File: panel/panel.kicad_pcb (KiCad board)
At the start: 2 copper layers, 60.4 x 128.4 mm, 48 parts

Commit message: Ver 2.0 of board.
Also major advances in code.
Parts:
- added H46: MountingHole, panel:3mmLED, F.Cu at (111.5, 59.5)
- added H47: MountingHole, panel:3mmLED, F.Cu at (111.5, 71.5)
- added H48: MountingHole, panel:3mmLED, F.Cu at (111.5, 83.5)
- added H49: MountingHole, panel:3mmLED, F.Cu at (111.5, 95.5)
- added H50: MountingHole, panel:3mmLED, F.Cu at (111.5, 109.5)
- added H51: MountingHole, panel:3mmLED, F.Cu at (111.5, 121.5)
- added H52: MountingHole, panel:3mmLED, F.Cu at (111.5, 133.5)
- added H53: MountingHole, panel:3mmLED, F.Cu at (111.5, 145.5)
- added H54: MountingHole, panel:3mmLED, F.Cu at (111.5, 64.5)
- added H55: MountingHole, panel:3mmLED, F.Cu at (111.5, 76.5)
- added H56: MountingHole, panel:3mmLED, F.Cu at (111.5, 88.5)
- added H57: MountingHole, panel:3mmLED, F.Cu at (111.5, 100.5)
- added H58: MountingHole, panel:3mmLED, F.Cu at (111.5, 114.5)
- added H59: MountingHole, panel:3mmLED, F.Cu at (111.5, 126.5)
- added H60: MountingHole, panel:3mmLED, F.Cu at (111.8, 138.5)
- added H61: MountingHole, panel:3mmLED, F.Cu at (111.5, 150.5)
- added H62: MountingHole, panel:3mmLED, F.Cu at (84.1, 125.7)
- added H63: MountingHole, panel:3mmLED, F.Cu at (84.1, 149.7)
- moved H2 10.2 mm to (108.2, 43.8)
- moved H3 10.2 mm to (108.2, 166.2)
- moved GR2 10.0 mm to (108.0, 158.3)
- moved H18 10.0 mm to (117.0, 53.0)
- moved H19 10.0 mm to (117.0, 157.0)
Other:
- board size 60.4 x 128.4 mm -> 70.8 x 128.4 mm
- board text added: "14 HP -- WiFi Enabled"
- board text added: "v2.0"
- board text removed: "12 HP -- WiFi Enabled"
- board text removed: "Clip"
- board text removed: "v1.0"

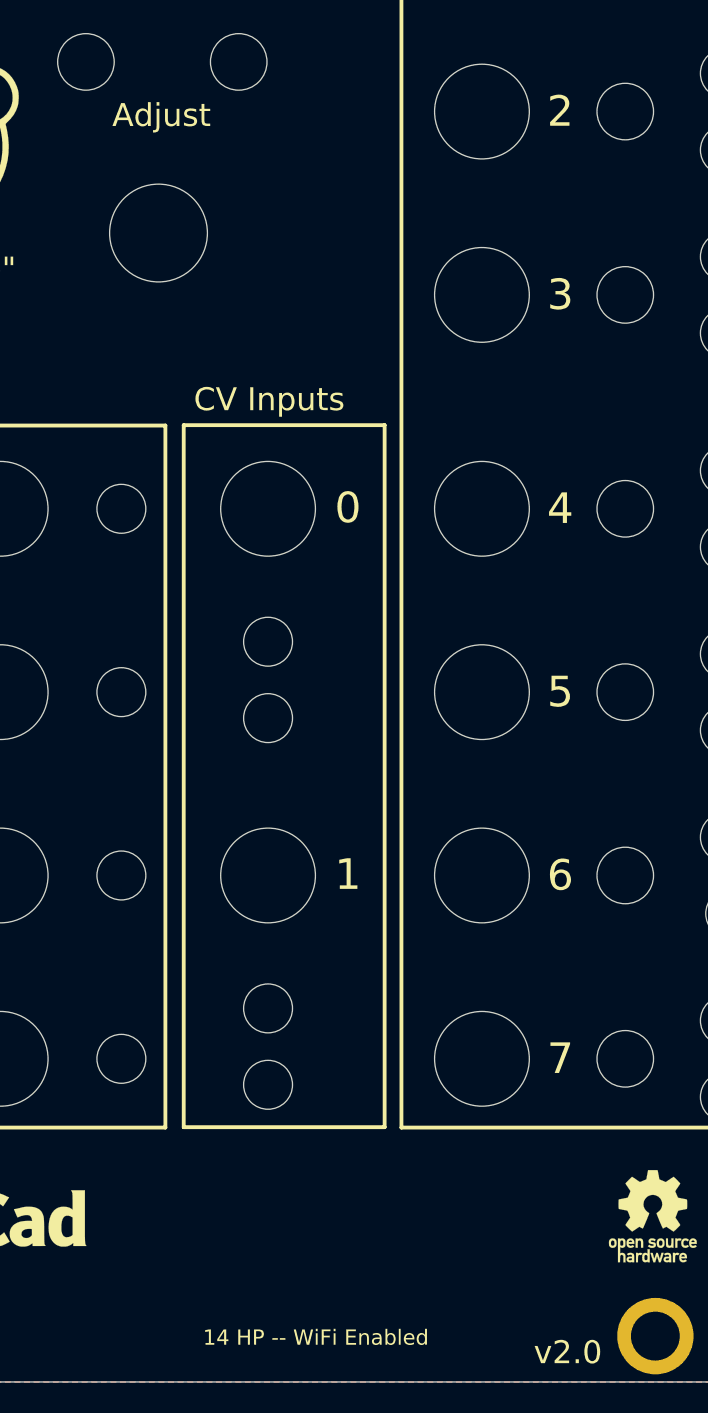
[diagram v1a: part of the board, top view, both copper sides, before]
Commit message: Software v2.2
Removes unneeded files.
Adds pre-flight handler in WiFi do_server();
Removes debug printouts.
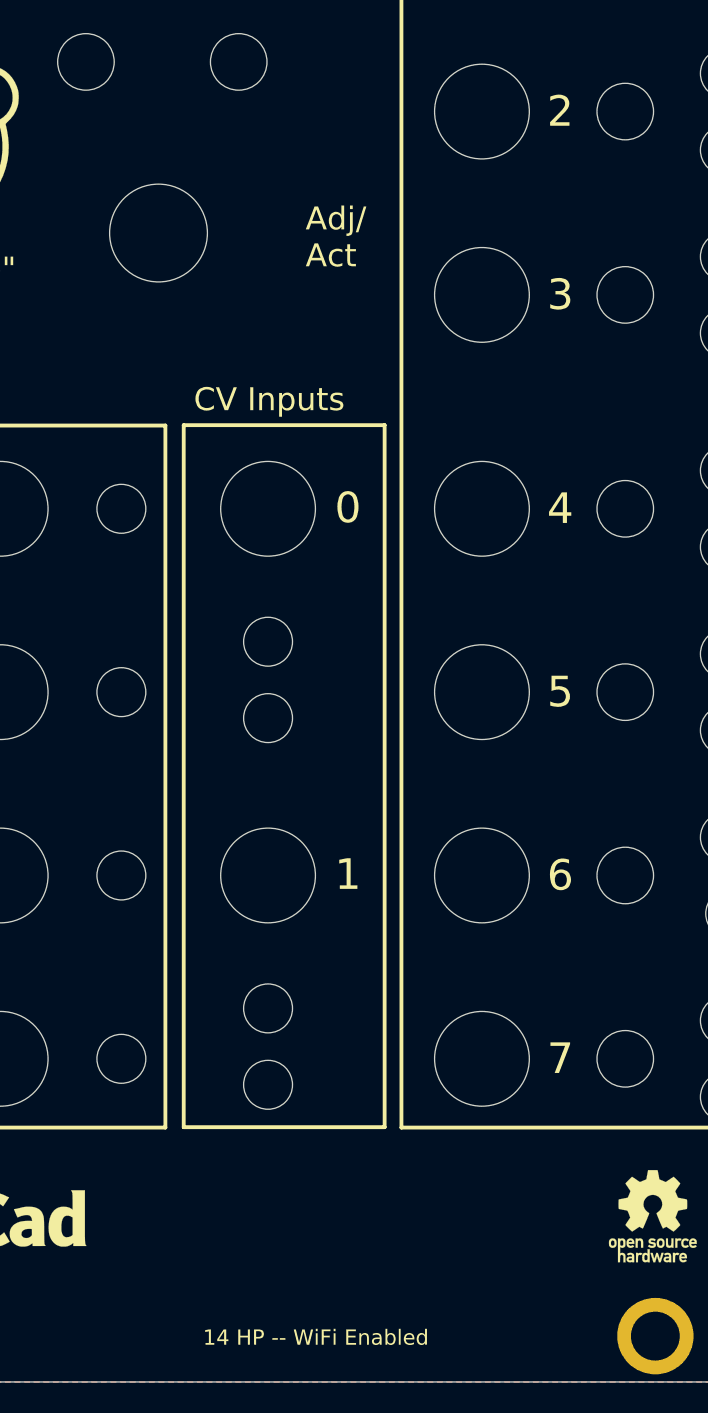
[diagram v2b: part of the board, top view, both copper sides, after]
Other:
- board text added: "Adj/ Act"
- board text added: "Greenface Labs {dblquote}The Bonkulator{dblquote} Panel: v1.1"
- board text removed: "Adjust"
- board text removed: "Greenface Labs {dblquote}The Bonkulator{dblquote} v1.0"
- board text removed: "v2.0"
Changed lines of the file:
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@@
   (gr_line (start 62.7 56.75) (end 62.7 71.75) (layer "Edge.Cuts") (width 0.05))
   (gr_line (start 88.7 71.75) (end 88.7 56.75) (layer "Edge.Cuts") (width 0.05))
-  (gr_text "Greenface Labs\n{dblquote}The Bonkulator{dblquote}\nv1.0" (at 85.75 162.5) (layer "B.SilkS")
+  (gr_text "Greenface Labs\n{dblquote}The Bonkulator{dblquote}\nPanel: v1.1" (at 85.75 162.5) (layer "B.SilkS")
     (effects (font (size 1.5 1.5) (thickness 0.25)) (justify mirror))
   )
@@
     (effects (font (size 2 2) (thickness 0.3)))
   )
-  (gr_text "Adjust" (at 75.9 86.25) (layer "F.SilkS")
-    (effects (font (size 1.5 1.5) (thickness 0.3)))
-  )
-  (gr_text "v2.0" (at 102.5 167.225) (layer "F.SilkS")
-    (effects (font (size 1.5 1.5) (thickness 0.15)))
+  (gr_text "Adj/\nAct" (at 85.325 94.225) (layer "F.SilkS")
+    (effects (font (size 1.5 1.5) (thickness 0.3)) (justify left))
   )
   (gr_text "<" (at 53.05 68 90) (layer "F.SilkS")

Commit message: Updates panel
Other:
- outline, holes or cut-outs redrawn
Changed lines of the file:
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@@
   )
   (paper "A4")
+  (title_block
+    (rev "2.1")
+  )
   (layers
     (0 "F.Cu" signal)
@@
     (pad "" np_thru_hole circle (at 1.27 0) (size 3.2 3.2) (drill 3.2) (layers *.Cu *.Mask))
   )
-  (gr_line (start 62.4 72.05) (end 62.4 56.45) (layer "F.SilkS") (width 0.5))
+  (gr_line (start 62.4 71) (end 62.4 56.45) (layer "F.SilkS") (width 0.5))
   (gr_rect (start 91.6 56.4) (end 119.55 152.5) (layer "F.SilkS") (width 0.25) (fill none))
   (gr_rect (start 51.1 106.55) (end 76.15 152.5) (layer "F.SilkS") (width 0.25) (fill none))
-  (gr_line (start 89 56.45) (end 89 72.05) (layer "F.SilkS") (width 0.5))
+  (gr_line (start 89 56.45) (end 89 71) (layer "F.SilkS") (width 0.5))
   (gr_rect (start 77.35 106.525) (end 90.5 152.475) (layer "F.SilkS") (width 0.25) (fill none))
   (gr_line (start 62.4 56.45) (end 89 56.45) (layer "F.SilkS") (width 0.5))
-  (gr_line (start 89 72.05) (end 62.4 72.05) (layer "F.SilkS") (width 0.5))
+  (gr_line (start 89 71.05) (end 62.4 71.05) (layer "F.SilkS") (width 0.5))
   (gr_line (start 50 50) (end 120.8 50) (layer "Dwgs.User") (width 0.1))
   (gr_line (start 120.8 40.75) (end 50 40.75) (layer "Edge.Cuts") (width 0.05))
@@
   (gr_line (start 50 169.15) (end 120.8 169.15) (layer "Edge.Cuts") (width 0.05))
   (gr_line (start 50 40.75) (end 50 169.15) (layer "Edge.Cuts") (width 0.05))
-  (gr_line (start 62.7 71.75) (end 88.7 71.75) (layer "Edge.Cuts") (width 0.05))
-  (gr_line (start 62.7 56.75) (end 62.7 71.75) (layer "Edge.Cuts") (width 0.05))
-  (gr_line (start 88.7 71.75) (end 88.7 56.75) (layer "Edge.Cuts") (width 0.05))
+  (gr_line (start 62.7 70.75) (end 88.7 70.75) (layer "Edge.Cuts") (width 0.05))
+  (gr_line (start 62.7 56.75) (end 62.7 70.75) (layer "Edge.Cuts") (width 0.05))
+  (gr_line (start 88.7 70.75) (end 88.7 56.75) (layer "Edge.Cuts") (width 0.05))
   (gr_text "Greenface Labs\n{dblquote}The Bonkulator{dblquote}\nPanel: v1.1" (at 85.75 162.5) (layer "B.SilkS")
     (effects (font (size 1.5 1.5) (thickness 0.25)) (justify mirror))

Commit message: Moves gerber to fab folder.
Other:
- board text removed: "Greenface Labs {dblquote}The Bonkulator{dblquote} Panel: v1.1"
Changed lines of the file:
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@@
       (drillshape 0)
       (scaleselection 1)
-      (outputdirectory "gerber/")
+      (outputdirectory "fab/gerber/")
     )
   )
@@
   (gr_line (start 62.7 56.75) (end 62.7 70.75) (layer "Edge.Cuts") (width 0.05))
   (gr_line (start 88.7 70.75) (end 88.7 56.75) (layer "Edge.Cuts") (width 0.05))
-  (gr_text "Greenface Labs\n{dblquote}The Bonkulator{dblquote}\nPanel: v1.1" (at 85.75 162.5) (layer "B.SilkS")
-    (effects (font (size 1.5 1.5) (thickness 0.25)) (justify mirror))
-  )
   (gr_text "Triggers" (at 56 105) (layer "F.SilkS")
     (effects (font (size 1.5 1.5) (thickness 0.3)))

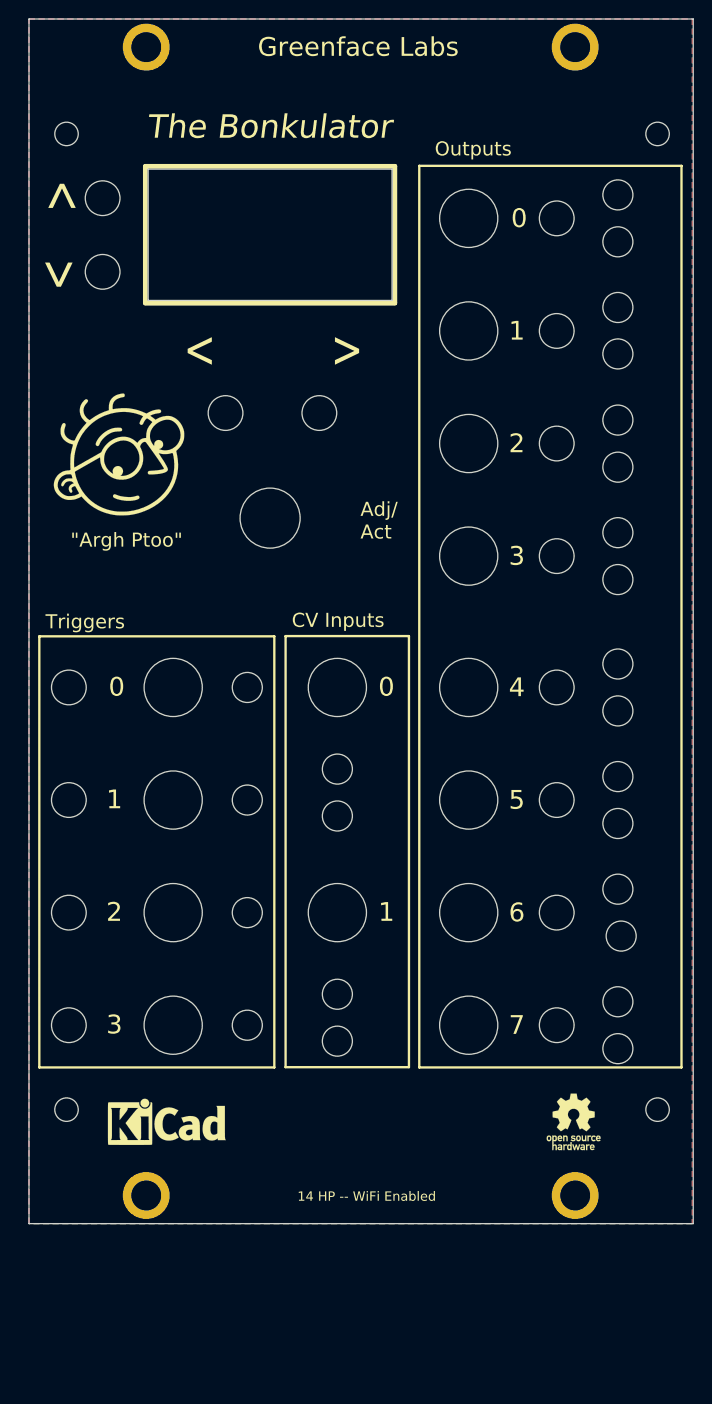
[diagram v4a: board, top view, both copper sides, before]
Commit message: Updates main board to 4.1, fixes panel LED that was off center.
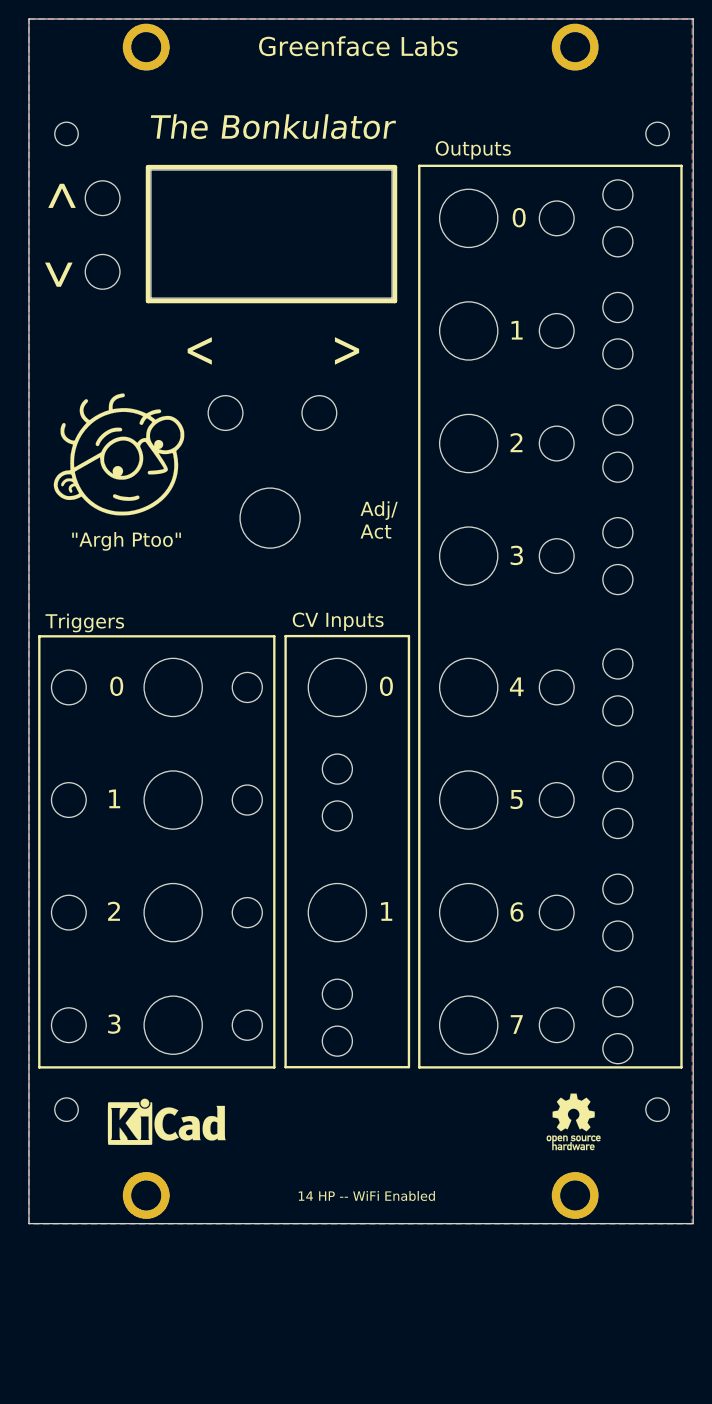
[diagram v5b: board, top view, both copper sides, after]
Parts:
- moved H60 0.35 mm to (111.5, 138.5)
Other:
- outline, holes or cut-outs redrawn
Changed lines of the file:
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@@
   )
   (footprint "panel:3mmLED" (layer "F.Cu")
-    (at 111.85 138.5)
+    (at 111.5 138.5)
     (descr "Mounting Hole 3.2mm, no annular, M3, DIN965")
     (tags "mounting hole 3.2mm no annular m3 din965")
@@
     (pad "" np_thru_hole circle (at 1.27 0) (size 3.2 3.2) (drill 3.2) (layers *.Cu *.Mask))
   )
-  (gr_line (start 62.4 71) (end 62.4 56.45) (layer "F.SilkS") (width 0.5))
+  (gr_line (start 62.7 70.8) (end 62.7 56.55) (layer "F.SilkS") (width 0.5))
   (gr_rect (start 91.6 56.4) (end 119.55 152.5) (layer "F.SilkS") (width 0.25) (fill none))
   (gr_rect (start 51.1 106.55) (end 76.15 152.5) (layer "F.SilkS") (width 0.25) (fill none))
-  (gr_line (start 89 56.45) (end 89 71) (layer "F.SilkS") (width 0.5))
+  (gr_line (start 89 56.55) (end 89 70.8) (layer "F.SilkS") (width 0.5))
   (gr_rect (start 77.35 106.525) (end 90.5 152.475) (layer "F.SilkS") (width 0.25) (fill none))
-  (gr_line (start 62.4 56.45) (end 89 56.45) (layer "F.SilkS") (width 0.5))
-  (gr_line (start 89 71.05) (end 62.4 71.05) (layer "F.SilkS") (width 0.5))
+  (gr_line (start 62.7 56.55) (end 89 56.55) (layer "F.SilkS") (width 0.5))
+  (gr_line (start 89 70.8) (end 62.7 70.8) (layer "F.SilkS") (width 0.5))
   (gr_line (start 50 50) (end 120.8 50) (layer "Dwgs.User") (width 0.1))
   (gr_line (start 120.8 40.75) (end 50 40.75) (layer "Edge.Cuts") (width 0.05))
-  (gr_line (start 88.7 56.75) (end 62.7 56.75) (layer "Edge.Cuts") (width 0.05))
+  (gr_line (start 88.7 56.85) (end 63 56.85) (layer "Edge.Cuts") (width 0.05))
   (gr_line (start 120.8 169.15) (end 120.8 40.75) (layer "Edge.Cuts") (width 0.05))
   (gr_line (start 50 169.15) (end 120.8 169.15) (layer "Edge.Cuts") (width 0.05))
   (gr_line (start 50 40.75) (end 50 169.15) (layer "Edge.Cuts") (width 0.05))
-  (gr_line (start 62.7 70.75) (end 88.7 70.75) (layer "Edge.Cuts") (width 0.05))
-  (gr_line (start 62.7 56.75) (end 62.7 70.75) (layer "Edge.Cuts") (width 0.05))
-  (gr_line (start 88.7 70.75) (end 88.7 56.75) (layer "Edge.Cuts") (width 0.05))
+  (gr_line (start 63 70.5) (end 88.7 70.5) (layer "Edge.Cuts") (width 0.05))
+  (gr_line (start 63 56.85) (end 63 70.5) (layer "Edge.Cuts") (width 0.05))
+  (gr_line (start 88.7 70.5) (end 88.7 56.85) (layer "Edge.Cuts") (width 0.05))
   (gr_text "Triggers" (at 56 105) (layer "F.SilkS")
     (effects (font (size 1.5 1.5) (thickness 0.3)))
@@
     (effects (font (size 1.5 1.5) (thickness 0.3)))
   )
-  (gr_text "The Bonkulator" (at 75.6 52.25) (layer "F.SilkS")
+  (gr_text "The Bonkulator" (at 75.8 52.35) (layer "F.SilkS")
     (effects (font (size 2.5 2.5) (thickness 0.25) italic))
   )

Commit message: Removes KiCAD logo, moves display outline
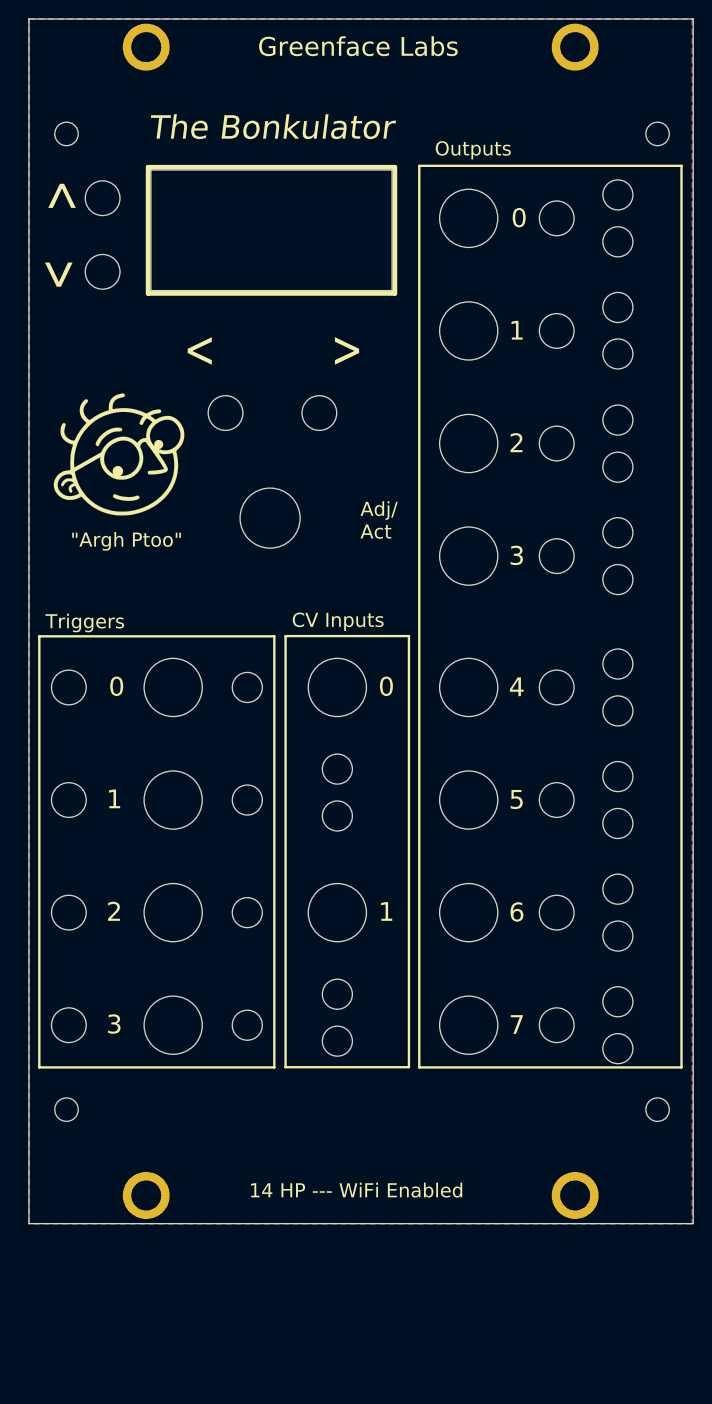
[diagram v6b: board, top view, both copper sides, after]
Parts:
- removed GR2: Logo_Open_Hardware_Small, Symbol:OSHW-Logo_5.7x6mm_SilkScreen
- removed GR3: small_logo, Symbol:KiCad-Logo_5mm_SilkScreen
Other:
- outline, holes or cut-outs redrawn
- board text added: "14 HP --- WiFi Enabled"
- board text removed: "14 HP -- WiFi Enabled"

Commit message: New front panel silkscreen
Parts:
- added GR2: Logo_Open_Hardware_Small, Symbol:OSHW-Logo_5.7x6mm_SilkScreen, F.Cu at (62.6, 159.6)
- added GR3: small_logo, panel:wifi, F.Cu at (108.2, 158.7)
- moved GR1 78.1 mm to (85.4, 161.3)
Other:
- board text added: "14 HP"
- board text added: "Adjust/Activate"
- board text added: "Push&Hold for Settings"
- board text added: "WiFi Enabled"
- board text removed: "14 HP --- WiFi Enabled"
- board text removed: "Adj/ Act"
- board text removed: "{dblquote}Argh Ptoo{dblquote}"
